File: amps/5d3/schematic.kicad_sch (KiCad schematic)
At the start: 43 parts, among them T2 PP : 8

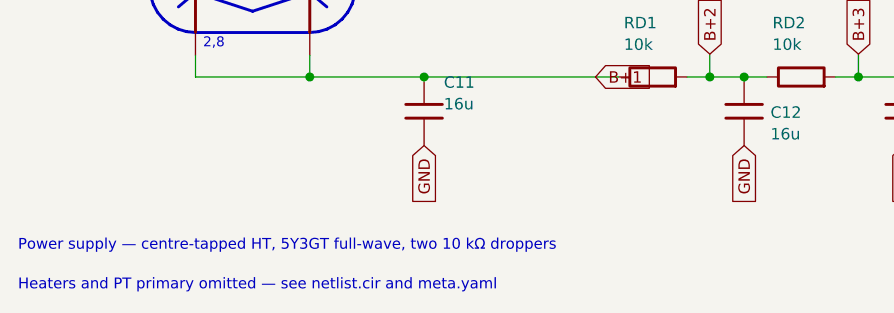
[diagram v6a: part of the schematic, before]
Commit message: Fix: schematic sheet notes no longer name repository files
Thirty-seven committed sheets rendered footnotes and section notes such as
"Heaters and PT primary omitted — see netlist.cir and meta.yaml" or
"excluded from netlist.cir (notes.md)" to visitors through KiCanvas. The
prose sweeps never counted sheets. Rewritten in the site's own words — the
netlist, the sources list, the circuit story, the parts list, the board
drawing — in 59 strings across 33 draw scripts, keeping every technical
claim as it was; the three tone sheets (6G4, 6G5, 6G6-B) are under repair
elsewhere and keep theirs for now. The sweep touched only strings passed to
the sheet's note, text, caption and footnote calls, never a path or a value.

Gates: check_schematics 40/0, connectivity 0 isolated pins;
verify_schematic_nets 40 clean; only the regenerated sheets and their served
copies changed.

Co-Authored-By: Claude Fable 5.1 <noreply@anthropic.com>
Claude-Session: https://claude.ai/code/session_01KBMfdh37HmCL2iWcBiL5J1
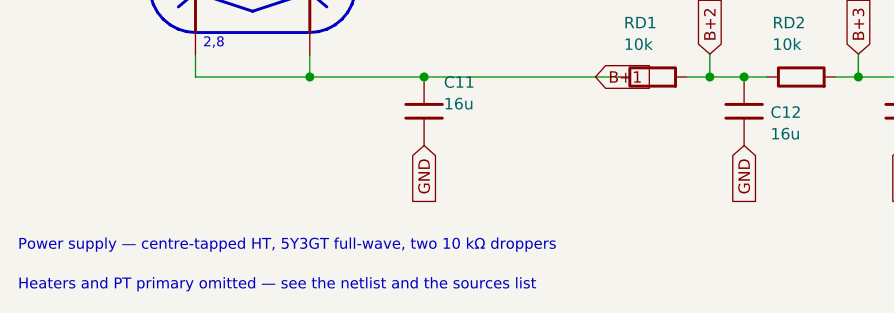
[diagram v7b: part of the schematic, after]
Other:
- note added: "Heaters and PT primary omitted — see the netlist and the sources list"
- note removed: "Heaters and PT primary omitted — see netlist.cir and meta.yaml"
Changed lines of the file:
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@@
   (text "Power supply — centre-tapped HT, 5Y3GT full-wave, two 10 kΩ droppers" (at 12.7 162.856 0)
     (effects (font (size 1.2 1.2)) (justify left)))
-  (text "Heaters and PT primary omitted — see netlist.cir and meta.yaml" (at 12.7 167.256 0)
+  (text "Heaters and PT primary omitted — see the netlist and the sources list" (at 12.7 167.256 0)
     (effects (font (size 1.2 1.2)) (justify left)))
   (sheet_instances (path "/" (page "1")))
